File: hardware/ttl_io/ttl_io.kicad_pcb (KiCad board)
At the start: 4 copper layers, 120 x 75 mm, 189 parts, among them J1 Conn_01x03_Male, J10 Conn_Coaxial, J11 Conn_Coaxial, J12 Conn_Coaxial, J13 Conn_02x08_Counter_Clockwise, J14 Conn_02x08_Counter_Clockwise, J2 AudioJack3, J3 USB_C_Receptacle_USB2.0, J4 Barrel_Jack_Switch, J5 Conn_Coaxial, J6 Conn_Coaxial, J7 Conn_Coaxial, J8 Conn_Coaxial, J9 Conn_Coaxial, SW1 SW_Push, SW2 SW_SPDT, SW3 SW_SPDT, U1 TPD2EUSB30, U10 74LVCH2T45DC, U11 74LVCH2T45DC, U12 74LVCH2T45DC, U13 74LVCH2T45DC, U14 74CBTLV3245, U15 SN74LVC1G14DRL, U16 74CBTLV3245, U17 74CBTLV3245, U18 74LVC1G04, U19 TXB0108DQSR, U2 ADUM4160, U3 RP2040, U4 W25Q16JVUXIQ, U5 74LVCH2T45DC, U6 74LVCH2T45DC, U7 74LVCH2T45DC, U8 LT3506, U9 74LVCH2T45DC, X1 ECS-TXO-2016

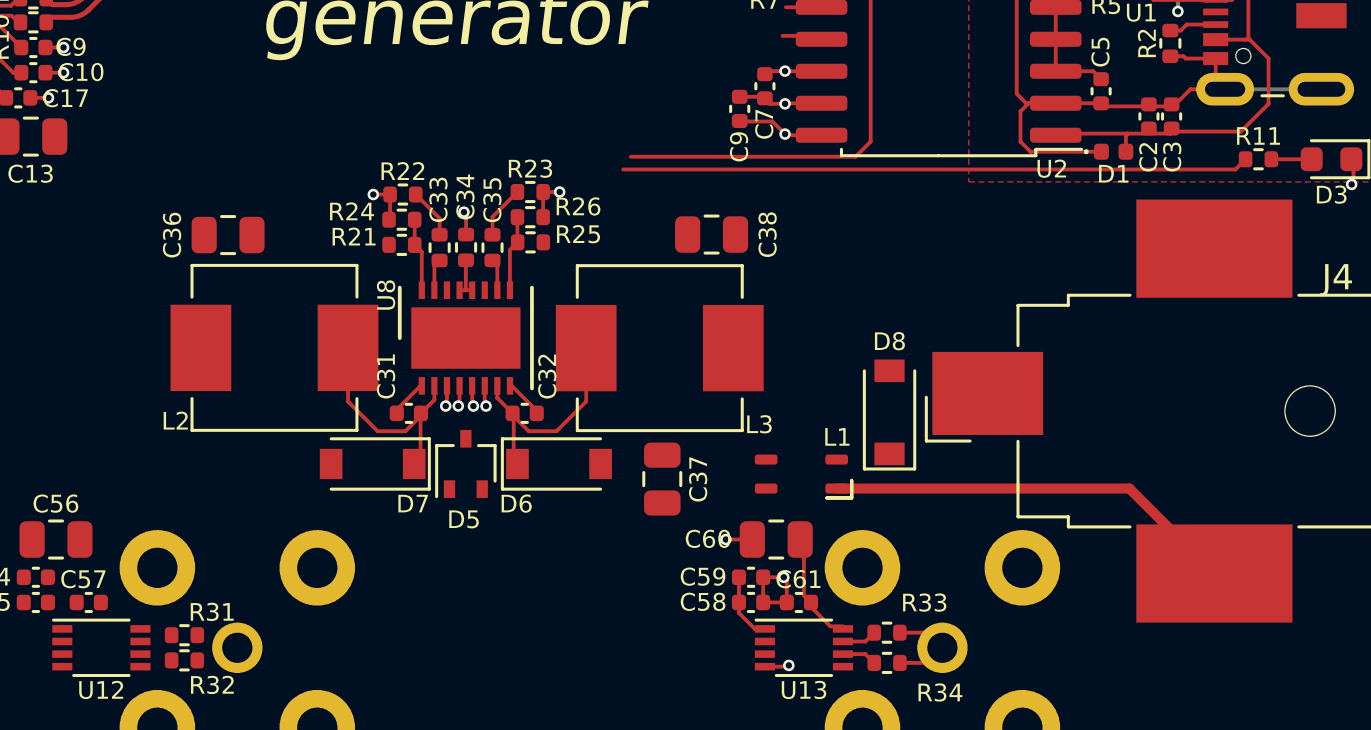
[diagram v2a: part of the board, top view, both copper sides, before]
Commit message: update power supply schematic/board
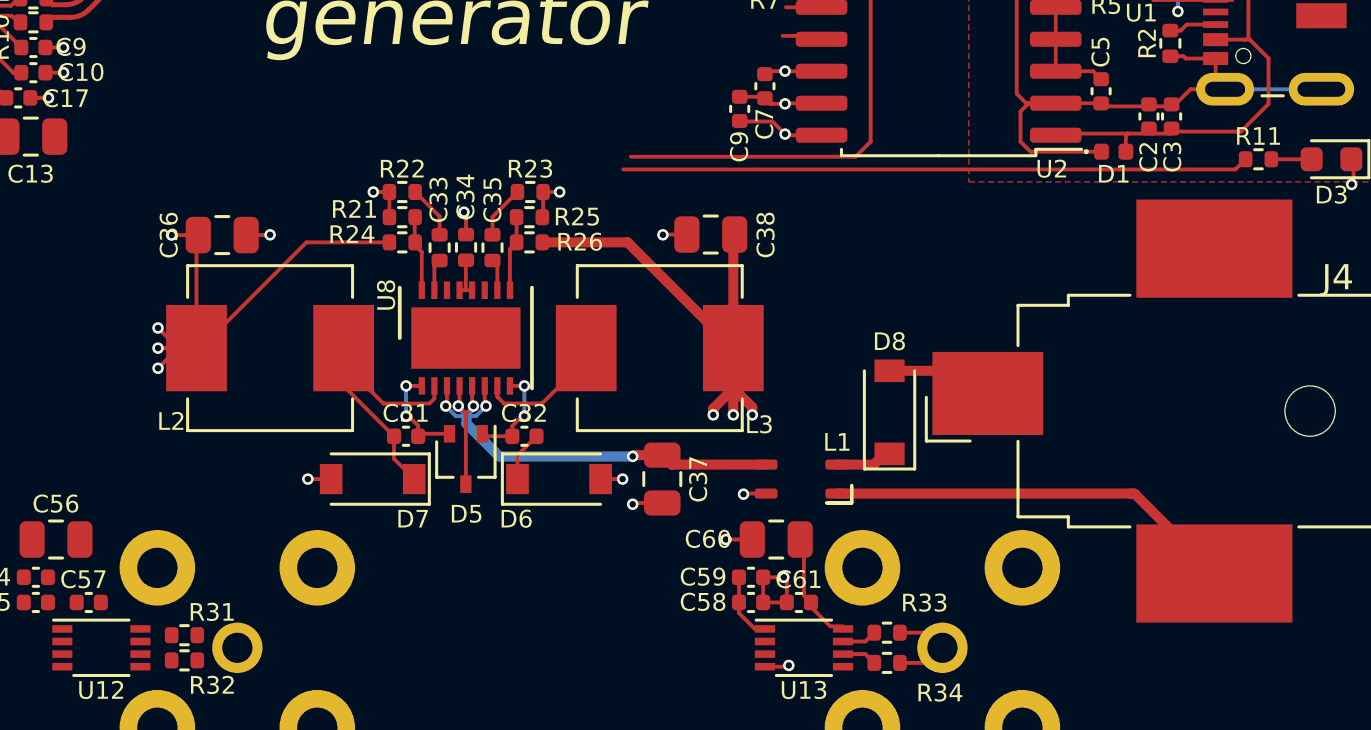
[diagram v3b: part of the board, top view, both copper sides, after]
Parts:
- moved R21 1.10 mm to (185.4, 89.9)
- moved R25 1.00 mm to (190.5, 89.9)
- moved R26 1.00 mm to (190.5, 90.9), turned to 0 degrees
- moved C31 0.92 mm to (185.6, 98.6), turned to 0 degrees
- moved C32 0.91 mm to (190.3, 98.6), turned to 180 degrees
- moved R24 0.90 mm to (185.4, 90.9)
- moved D6 0.60 mm to (191.7, 100.3)
- moved D7 0.60 mm to (184.3, 100.3)
- moved C36 0.23 mm to (178.3, 90.6)
- moved D5 0.20 mm to (188.0, 99.5), turned to -90 degrees
- moved L1 0.20 mm to (201.3, 100.3)
- moved L2 0.18 mm to (180.2, 95.1)
- moved R22 0.10 mm to (185.4, 88.9)
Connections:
- C35 pad 1: Net-(U8-VC2) -> Net-(U8-PG1)
- R21 pad 2: +3V3 -> GND
- R24 pad 2: GND -> +3V3
- R25 pad 1: +5V -> GND
- R26 pad 1: GND -> Net-(U8-FB2)
- R26 pad 2: Net-(U8-FB2) -> +5V
- U8 pad 10: Net-(U8-VC2) -> Net-(U8-PG1)
- U8 pad 14: unconnected-(U8-PG1-Pad14) -> Net-(U8-PG1)
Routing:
- net +5V: track 4.45 -> 26.9 mm, vias 0 -> 3
- net VIN1: track 3.28 -> 22.8 mm, vias 4 -> 5
- net +3V3: track 46.7 -> 66.2 mm, vias 17 -> 21
- net GND: track 32.5 -> 38.4 mm, vias 24 -> 30
- net +12V: track 0.00 -> 4.27 mm
- net Net-(U8-BOOST1): track 1.53 -> 4.17 mm, vias 0 -> 2
- net Net-(D7-K): track 9.30 -> 11.8 mm
- net Net-(U8-BOOST2): track 1.58 -> 4.06 mm, vias 0 -> 2
- net Net-(D8-K): track 0.00 -> 2.28 mm
- net Net-(D6-K): track 9.30 -> 7.26 mm
- net Net-(U8-VC2): track 1.26 -> 0.00 mm
- net Net-(U8-PG1): track 0.00 -> 1.26 mm

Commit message: annotate bus logic on schematic
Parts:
- moved G2 4.97 mm to (134.0, 80.5)
- moved R36 1.50 mm to (118.0, 88.0)
- moved R35 1.49 mm to (116.8, 88.0)
- moved R37 1.49 mm to (119.2, 88.0)
- moved R38 1.49 mm to (120.4, 88.0)
- moved R39 1.49 mm to (121.6, 88.0)
- moved R40 1.49 mm to (122.8, 88.0)
- moved R41 1.49 mm to (124.0, 88.0)
- moved R42 1.49 mm to (125.2, 88.0)
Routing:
- net +3V3: track 66.2 -> 72.4 mm, vias 21 -> 29
- net /EXT_DIR1: track 32.7 -> 31.2 mm
- net /EXT_DIR7: track 42.3 -> 40.8 mm
- net /EXT_DIR6: track 40.2 -> 38.7 mm
- net /EXT_DIR5: track 38.4 -> 37.0 mm
- net /EXT_DIR4: track 37.0 -> 35.5 mm
- net /EXT_DIR3: track 35.6 -> 34.1 mm
- net /EXT_DIR2: track 34.2 -> 32.7 mm
- net /EXT_DIR0: track 32.4 -> 30.9 mm
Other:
- board text added: "External Input Logic Level Selection:"
- board text added: "↑ 3.3V ↓ 5V"

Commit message: update pcb
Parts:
- removed the D3 at (215.9, 77.7)
- added C78: 100nF, Capacitor_SMD:C_0402_1005Metric, F.Cu at (216.1, 55.8)
- added C79: 100nF, Capacitor_SMD:C_0402_1005Metric, F.Cu at (216.1, 58.3)
- added C80: 1uF, Capacitor_SMD:C_0402_1005Metric, F.Cu at (217.1, 55.8)
- added C81: 1uF, Capacitor_SMD:C_0402_1005Metric, F.Cu at (217.1, 58.3)
- added R49: 1K, Resistor_SMD:R_0402_1005Metric, F.Cu at (233.8, 59.7)
- added R50: 1K, Resistor_SMD:R_0402_1005Metric, F.Cu at (243.7, 59.7)
- added R51: 1K, Resistor_SMD:R_0402_1005Metric, F.Cu at (244.2, 52.3)
- added R52: 10K, Resistor_SMD:R_0402_1005Metric, F.Cu at (113.0, 80.0)
- added REF**: MountingHole_2.2mm_M2_ISO7380, MountingHole:MountingHole_2.2mm_M2_ISO7380, F.Cu at (217.9, 111.0)
- added REF**: MountingHole_2.2mm_M2_ISO7380, MountingHole:MountingHole_2.2mm_M2_ISO7380, F.Cu at (111.9, 50.0)
- added REF**: MountingHole_2.2mm_M2_ISO7380, MountingHole:MountingHole_2.2mm_M2_ISO7380, F.Cu at (217.9, 50.0)
- added REF**: MountingHole_2.2mm_M2_ISO7380, MountingHole:MountingHole_2.2mm_M2_ISO7380, F.Cu at (111.9, 111.0)
- R11, R12: value 680 -> 1K
- U18: value 74LVC1G04 -> SN74LVC1G14DRL; footprint Package_TO_SOT_SMD:SOT-23-5 -> Package_TO_SOT_SMD:SOT-553
- U19: value TXB0108DQSR -> TXB0108; footprint Package_SON:USON-20_2x4mm_P0.4mm -> Package_SO:TSSOP-20_4.4x6.5mm_P0.65mm
- moved C77 27.4 mm to (212.4, 53.8)
- moved R48 25.2 mm to (214.4, 53.8)
- moved R44 24.2 mm to (218.1, 58.3), turned to -90 degrees
- moved U15 24.2 mm to (214.5, 55.5), turned to -90 degrees
- moved C70 21.1 mm to (235.2, 51.3)
- moved C71 21.1 mm to (235.2, 52.3)
- moved U18 16.2 mm to (214.5, 58.0), turned to -90 degrees
- moved R47 12.9 mm to (233.8, 58.7), turned to 180 degrees
- moved C75 11.6 mm to (243.7, 61.7)
- moved C74 11.3 mm to (244.2, 54.3)
- moved R45 11.3 mm to (244.2, 53.3)
- moved D9 10.4 mm to (223.2, 49.9)
- moved R46 10.1 mm to (243.7, 60.7)
- moved D12 9.46 mm to (242.7, 52.8), turned to 90 degrees
- moved D10 9.14 mm to (242.2, 60.2), turned to 90 degrees
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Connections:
- D11 pad 2: EXT_CTRL -> Net-(D11-A)
- D12 pad 2: Net-(D11-K) -> Net-(D12-A)
- R46 pad 2: Net-(D10-A) -> /Bus Selection/BUS_STATE
- U18 pad 1: (no net) -> unconnected-(U18-NC-Pad1)
- U18 pad 4: Net-(D10-A) -> /Bus Selection/BUS_STATE
- U3 pad 4: unconnected-(U3-GPIO2-Pad4) -> /Bus Selection/BUS_STATE
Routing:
- net +3V3: track 72.4 -> 117.5 mm, vias 29 -> 43
- net /Harp Core Rp2040 + isolated USB/DD-: track 3.05 -> 29.0 mm
- net /Harp Core Rp2040 + isolated USB/QSPI_CS: track 14.7 -> 40.4 mm
- net /Harp Core Rp2040 + isolated USB/DD+: track 3.46 -> 29.0 mm
- net GND: track 38.4 -> 57.2 mm, vias 30 -> 49
- net Net-(D9-K): track 0.00 -> 17.5 mm
- net /TTL0: track 0.00 -> 10.7 mm
- net /TTL1: track 1.07 -> 11.2 mm
- net /TTL2: track 0.00 -> 9.59 mm
- net /TTL3: track 15.8 -> 24.9 mm
- net /TTL4: track 0.00 -> 7.97 mm
- net /TTL5: track 0.00 -> 7.43 mm
- net Net-(D9-A): track 0.00 -> 7.41 mm, vias 0 -> 2
- net /TTL6: track 0.00 -> 6.90 mm
- net /TTL7: track 0.00 -> 6.36 mm
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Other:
- board text added: "3.3V ↑ ↓ 5V"
- board text added: "Ext I/O mode: TTL input/output controlled by pins on the board edge. (Orange LED On.) USB I/O mode: TTL input/output controlled by software over USB interface. (Orange LED Off.)"
- board text added: "Ext I/O ↑ ↓ USB I/O"
- board text added: "External Input Logic Level Selection Switch"
- board text added: "cuTTLfish: square wave generator"
- board text added: "v0.1.0, Jan 3, 2024"
- board text removed: "External Input Logic Level Selection:"
- board text removed: "TTL Square Wave Squid"
- board text removed: "cuTTLfish: octal square wave generator"
- board text removed: "v0.1.0, Nov 7, 2023"
- board text removed: "↑ 3.3V ↓ 5V"

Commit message: update pcb
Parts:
- removed C70: 100nF, Capacitor_SMD:C_0402_1005Metric
- removed C71: 1uF, Capacitor_SMD:C_0402_1005Metric
- moved C74 47.1 mm to (197.9, 63.2)
- moved D12 47.1 mm to (196.4, 61.7)
- moved R45 47.1 mm to (197.9, 62.2)
- moved R51 47.1 mm to (197.9, 61.2)
- moved C76 41.6 mm to (192.3, 63.2)
- moved D11 41.6 mm to (190.8, 61.8)
- moved R47 41.6 mm to (192.3, 61.2)
- moved R49 41.6 mm to (192.3, 62.2), turned to 180 degrees
- moved C75 40.1 mm to (203.7, 63.3)
- moved D10 40.1 mm to (202.2, 61.8)
- moved R46 40.1 mm to (203.7, 62.3)
- moved R50 40.1 mm to (203.7, 61.3)
- moved C73 39.8 mm to (110.0, 84.6)
- moved C8 22.0 mm to (177.1, 77.5)
- moved C13 7.70 mm to (178.2, 85.0), turned to 90 degrees
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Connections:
- C72 pad 2: +5V -> Net-(SW3-B)
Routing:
- net ~{EXT_CTRL}: track 0.00 -> 87.5 mm
- net /Bus Selection/BUS_STATE: track 2.53 -> 65.8 mm
- net /Harp Core Rp2040 + isolated USB/HARP_CLK_SYNC: track 1.37 -> 60.6 mm, vias 1 -> 2
- net ~{HARP_CTRL}: track 0.00 -> 47.0 mm
- net EXT_CTRL: track 1.25 -> 47.0 mm, vias 1 -> 2
- net Net-(D11-K): track 1.31 -> 28.7 mm
- net Net-(U3-GPIO24): track 31.5 -> 58.0 mm, vias 0 -> 2
- net Net-(U3-GPIO25): track 42.6 -> 67.6 mm
- net +3V3: track 117.5 -> 135.1 mm, vias 43 -> 44
- net GND: track 57.2 -> 64.4 mm, vias 49 -> 57
- net Net-(SW3-B): track 43.1 -> 45.0 mm
- net Net-(D11-A): track 0.00 -> 1.00 mm
- net Net-(D10-A): track 0.00 -> 1.00 mm
- net Net-(D12-A): track 0.00 -> 0.99 mm
- net +5V: track 28.4 -> 29.4 mm
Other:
- board text added: "TODO: Switch BOOTSEL switch for washable variant."
- board text removed: "Setup Notes: • Slide the switch <DIRECTION> to enable USB control of the BNC connections. • Slide the switch <DIRECTION> to enable external control of the BNC connections."
- board text removed: "TODO: TVS diodes on all BNC inputs? TODO: Switch BOOTSEL switch for washable variant."
